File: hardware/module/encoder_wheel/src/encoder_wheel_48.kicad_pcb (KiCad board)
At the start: 2 copper layers, 74 x 74 mm, 2 parts

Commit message: Remade controller hardware in KiCad.
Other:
- board text added: "Openflap Encoder Wheel 48 positions"
- board text removed: "Openflap Encoder Wheel 48 positions 1/4 Offset"
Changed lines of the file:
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@@
 		(fp_poly
 			(pts
-				(xy -7.206369 30.8754) (xy -6.1979 31.094248) (xy -5.181581 31.280407) (xy -4.158204 31.43352) (xy -3.128563 31.553274)
+				(xy -7.206369 30.8754) (xy -6.1979 31.094248) (xy -5.181581 31.280408) (xy -4.158204 31.43352) (xy -3.128563 31.553274)
 				(xy -2.09345 31.639325) (xy -1.053658 31.691338) (xy -0.009979 31.708977) (xy -0.010895 33.703964)
 				(xy -1.11983 33.684381) (xy -2.2247 33.628316) (xy -3.324662 33.536128) (xy -4.418873 33.408173)
@@
 		(fp_poly
 			(pts
-				(xy 17.797251 -28.611602) (xy 18.260854 -28.318664) (xy 18.719893 -28.018081) (xy 19.174257 -27.709896)
+				(xy 17.797259 -28.611602) (xy 18.260854 -28.318664) (xy 18.719893 -28.018081) (xy 19.174257 -27.709896)
 				(xy 19.623839 -27.394155) (xy 20.068535 -27.070899) (xy 20.508239 -26.740174) (xy 20.942845 -26.402024)
 				(xy 21.372248 -26.056491) (xy 21.796343 -25.70362) (xy 22.215024 -25.343454) (xy 22.628185 -24.976039)
@@
 				(xy -16.136141 -21.027847) (xy -17.499432 -19.90962) (xy -18.775807 -18.711547) (xy -19.963051 -17.438974)
 				(xy -21.058953 -16.097244) (xy -22.0613 -14.691704) (xy -22.967879 -13.227699) (xy -23.776477 -11.710572)
-				(xy -24.484888 -10.145669) (xy -25.09088 -8.538336) (xy -25.592259 -6.893916) (xy -25.986807 -5.217756)
+				(xy -24.484889 -10.145669) (xy -25.09088 -8.538336) (xy -25.592259 -6.893916) (xy -25.986807 -5.217756)
 				(xy -26.272311 -3.515199) (xy -26.446558 -1.791591) (xy -26.507335 -0.052276) (xy -26.452429 1.697399)
 				(xy -26.279629 3.452091) (xy -28.260296 3.712608) (xy -28.444349 1.827105) (xy -28.501782 -0.053366)
@@
 				(xy -15.841457 -27.459876) (xy -16.841551 -29.192376) (xy -16.367876 -29.459985) (xy -15.888613 -29.720766)
 				(xy -15.403774 -29.974596) (xy -14.913372 -30.221354) (xy -14.417419 -30.460919) (xy -13.915927 -30.69317)
-				(xy -13.40891 -30.917985) (xy -12.896379 -31.135235) (xy -12.378796 -31.344652) (xy -11.859762 -31.544775)
+				(xy -13.40891 -30.917985) (xy -12.896379 -31.13523) (xy -12.378796 -31.344652) (xy -11.859762 -31.544775)
 				(xy -11.339373 -31.735684) (xy -10.817722 -31.917451) (xy -10.294903 -32.090151) (xy -9.771009 -32.253855)
 				(xy -9.246134 -32.408637) (xy -8.720371 -32.554569)
@@
 				(xy 26.681543 -10.020213) (xy 26.999836 -9.129266) (xy 27.28667 -8.234289) (xy 27.542362 -7.335921)
 				(xy 27.76723 -6.4348) (xy 27.96159 -5.531562) (xy 28.12576 -4.626846) (xy 28.260056 -3.721291) (xy 26.278908 -3.460571)
-				(xy 26.153379 -4.302066) (xy 26.000146 -5.142892) (xy 25.818912 -5.982438) (xy 25.609381 -6.820136)
+				(xy 26.153379 -4.302066) (xy 26.000146 -5.142894) (xy 25.818912 -5.982438) (xy 25.609381 -6.820136)
 				(xy 25.371258 -7.655388) (xy 25.104248 -8.487605) (xy 24.808054 -9.316196) (xy 24.48238 -10.140572)
 				(xy 23.928524 -11.387747) (xy 23.318981 -12.592352) (xy 22.655915 -13.753488) (xy 21.941492 -14.870261)
@@
 				(xy -18.969452 14.546986) (xy -20.554886 15.763035) (xy -21.049875 15.095393) (xy -21.525162 14.40912)
 				(xy -21.980135 13.704429) (xy -22.414179 12.981528) (xy -22.82668 12.240629) (xy -23.217026 11.481943)
-				(xy -23.58461 10.705679) (xy -23.928797 9.912048) (xy -24.407274 8.668743) (xy -24.817777 7.416073)
+				(xy -23.584615 10.705679) (xy -23.928797 9.912048) (xy -24.407274 8.668743) (xy -24.817777 7.416073)
 				(xy -25.161191 6.156172) (xy -25.438399 4.891176) (xy -25.650286 3.623219) (xy -25.797736 2.354438)
 				(xy -25.881634 1.086967) (xy -25.902863 -0.17706) (xy -25.86231 -1.435506) (xy -25.760857 -2.686236)
@@
 				(xy -19.302546 -17.272174) (xy -18.441366 -18.190706) (xy -17.532553 -19.069496) (xy -16.57699 -19.906408)
 				(xy -15.575563 -20.699309) (xy -14.529156 -21.446063) (xy -13.438653 -22.144535) (xy -12.304939 -22.792589)
-				(xy -11.128897 -23.388092) (xy -9.911413 -23.928913) (xy -9.911417 -23.928914) (xy -9.91142 -23.928922)
+				(xy -11.128897 -23.388092) (xy -9.911413 -23.928919) (xy -9.911417 -23.928914) (xy -9.91142 -23.928922)
 				(xy -9.911423 -23.92893) (xy -9.911426 -23.928937) (xy -9.911432 -23.928953) (xy -9.911438 -23.928968)
 				(xy -9.106097 -24.247061) (xy -8.296496 -24.536291) (xy -7.483219 -24.796944) (xy -6.66685 -25.029302)
-				(xy -5.847973 -25.233652) (xy -5.027173 -25.410284) (xy -4.205034 -25.559461) (xy -3.382141 -25.68149)
+				(xy -5.847973 -25.233652) (xy -5.027173 -25.410286) (xy -4.205034 -25.559461) (xy -3.382141 -25.68149)
 			)
 			(stroke
@@
 				(xy 11.253323 14.944536) (xy 11.977266 14.37219) (xy 12.667957 13.768177) (xy 13.324763 13.134026)
 				(xy 13.947052 12.471264) (xy 14.534191 11.781417) (xy 15.085548 11.066013) (xy 15.60049 10.326579)
-				(xy 16.078383 9.564643) (xy 16.518597 8.781724) (xy 16.920498 7.979371) (xy 17.283453 7.15909) (xy 17.60683 6.322415)
+				(xy 16.078383 9.564643) (xy 16.518597 8.78172) (xy 16.920498 7.979371) (xy 17.283453 7.15909) (xy 17.60683 6.322415)
 				(xy 17.889997 5.470874) (xy 18.13232 4.605994) (xy 18.333167 3.729302) (xy 18.491906 2.842324) (xy 18.607903 1.94659)
 				(xy 18.680527 1.043625) (xy 18.709145 0.134957) (xy 18.693124 -0.777888) (xy 18.631831 -1.69338)
@@
 				(xy 18.30925 10.899392) (xy 18.810685 10.008145) (xy 19.268541 9.094758) (xy 19.682098 8.160969)
 				(xy 21.518124 8.921875) (xy 21.065488 9.944101) (xy 20.564486 10.944026) (xy 20.015909 11.919733)
-				(xy 19.420559 12.869301) (xy 18.779225 13.790814) (xy 18.092703 14.682351) (xy 17.361781 15.541994)
+				(xy 19.420559 12.869301) (xy 18.779225 13.790814) (xy 18.092703 14.682351) (xy 17.361778 15.541994)
 				(xy 16.587275 16.367825) (xy 15.769959 17.157924) (xy 14.910635 17.910373) (xy 14.010097 18.623254)
 				(xy 13.06914 19.294647) (xy 12.088559 19.922634) (xy 11.06915 20.505296) (xy 10.011706 21.040714)
@@
 		(layer "Edge.Cuts")
 	)
-	(gr_text "Openflap\nEncoder Wheel\n48 positions\n1/4 Offset"
+	(gr_text "Openflap\nEncoder Wheel\n48 positions"
 		(at 101 78 0)
 		(layer "B.SilkS")

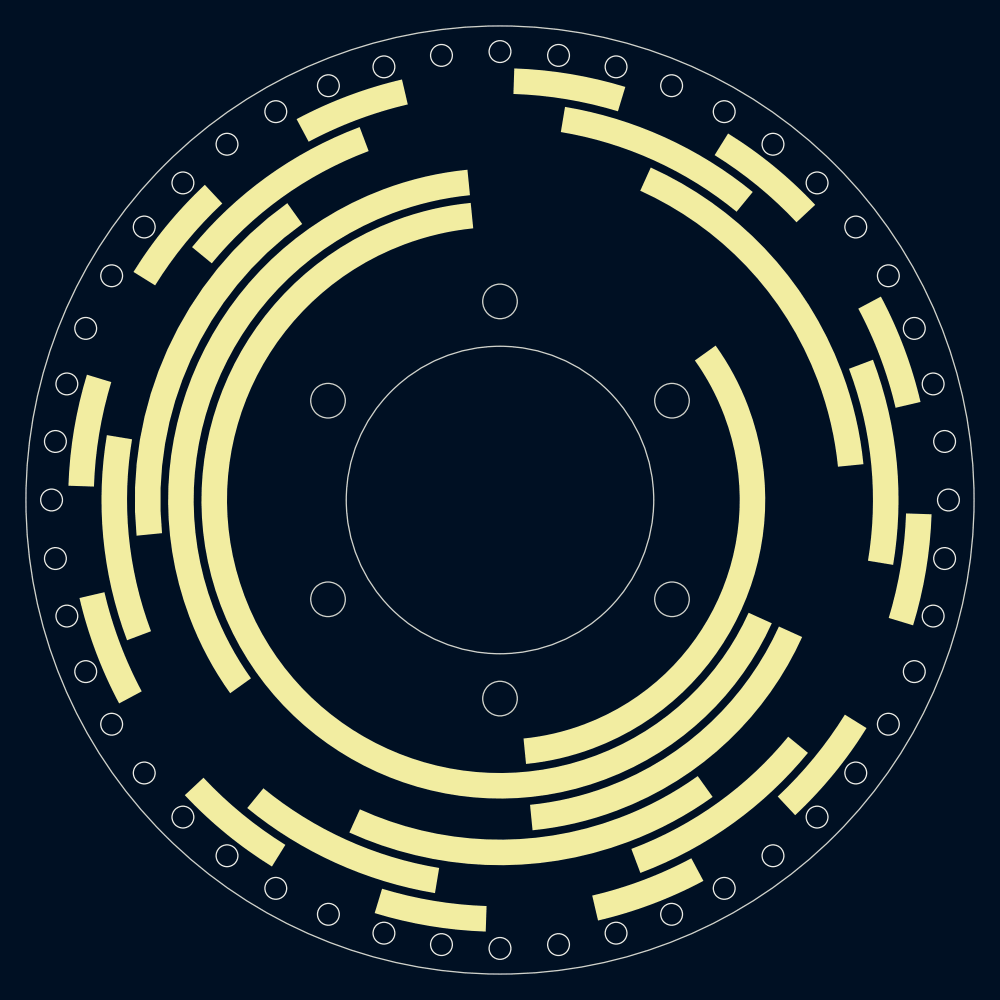
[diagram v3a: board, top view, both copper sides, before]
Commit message: offset encoder pattern so inner trace does not line up with fasteners
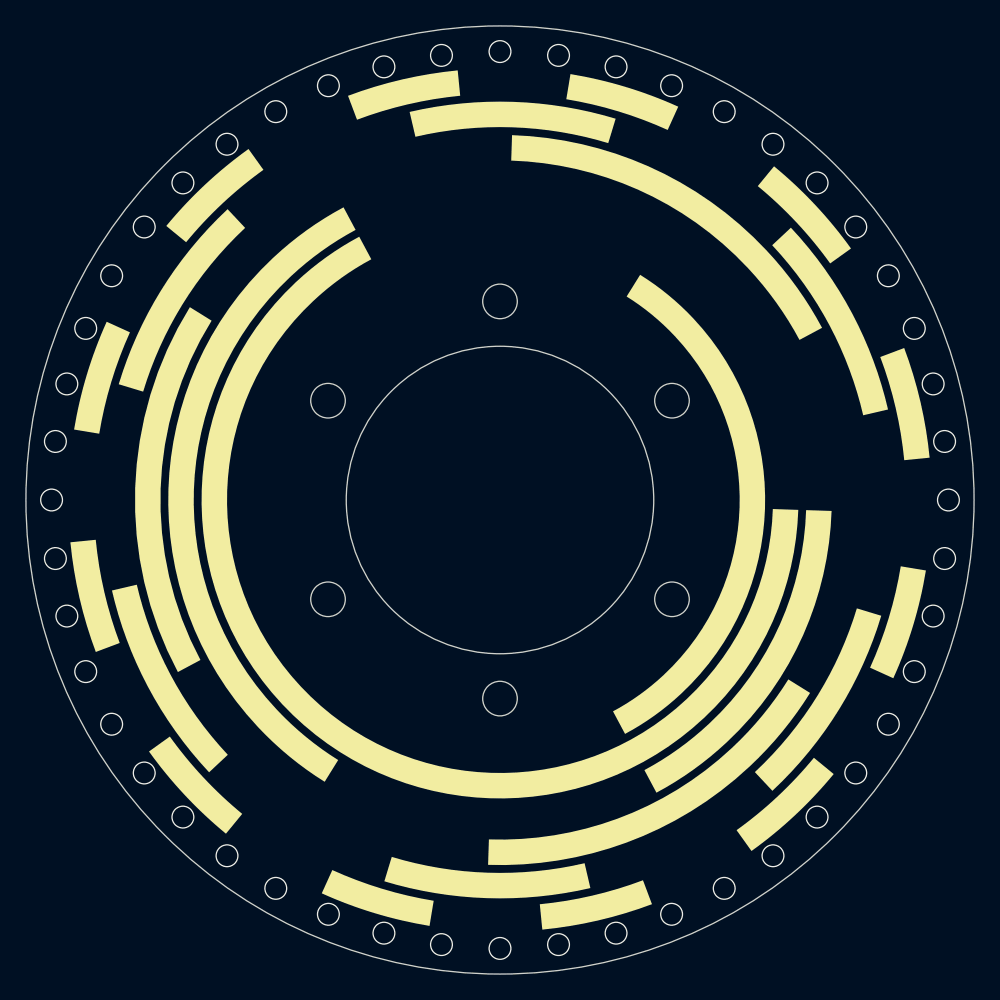
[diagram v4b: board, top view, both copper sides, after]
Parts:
- turned EncoderPattern to 20.625 degrees

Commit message: changed encoder offset from 1/4 to 1/2
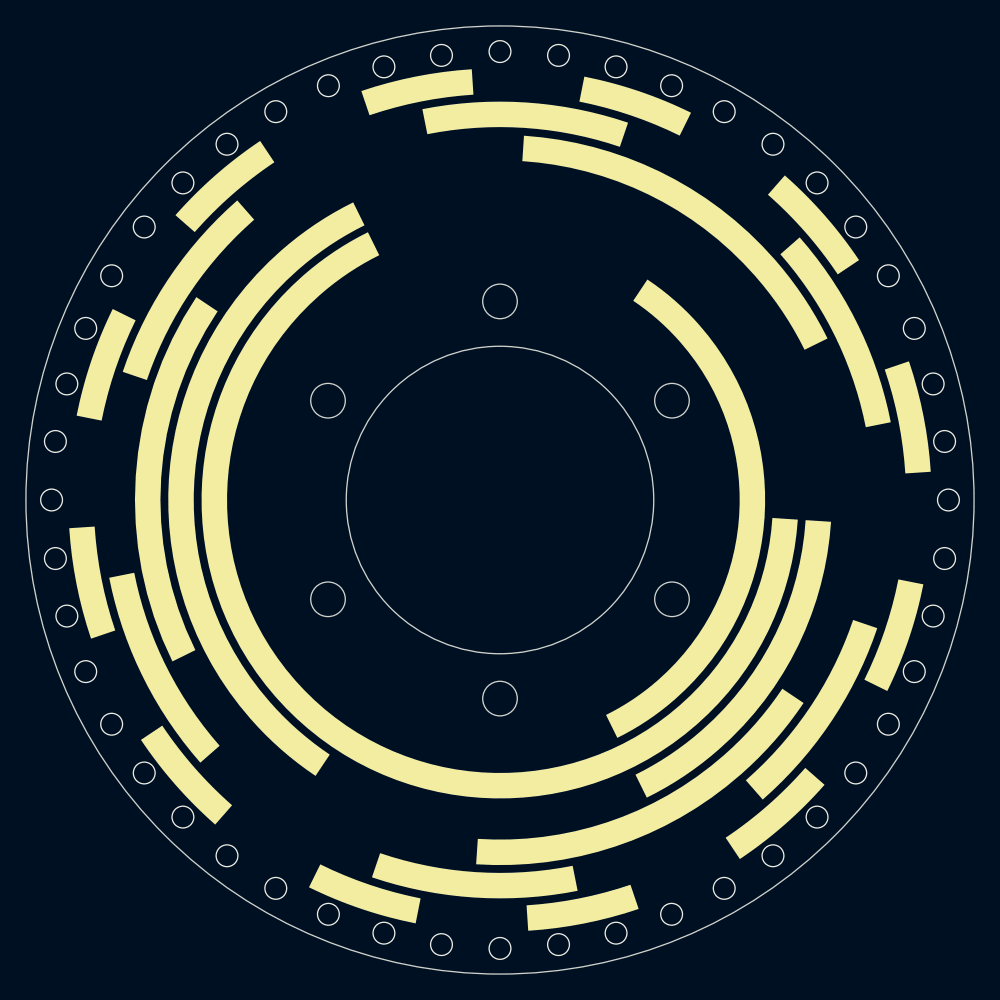
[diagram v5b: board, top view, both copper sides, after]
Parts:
- turned EncoderPattern to 18.75 degrees
